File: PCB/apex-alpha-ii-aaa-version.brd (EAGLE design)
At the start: 13.1 x 74.7 mm, 31 parts, among them IC1 CC430F5135, Y1 26MHz

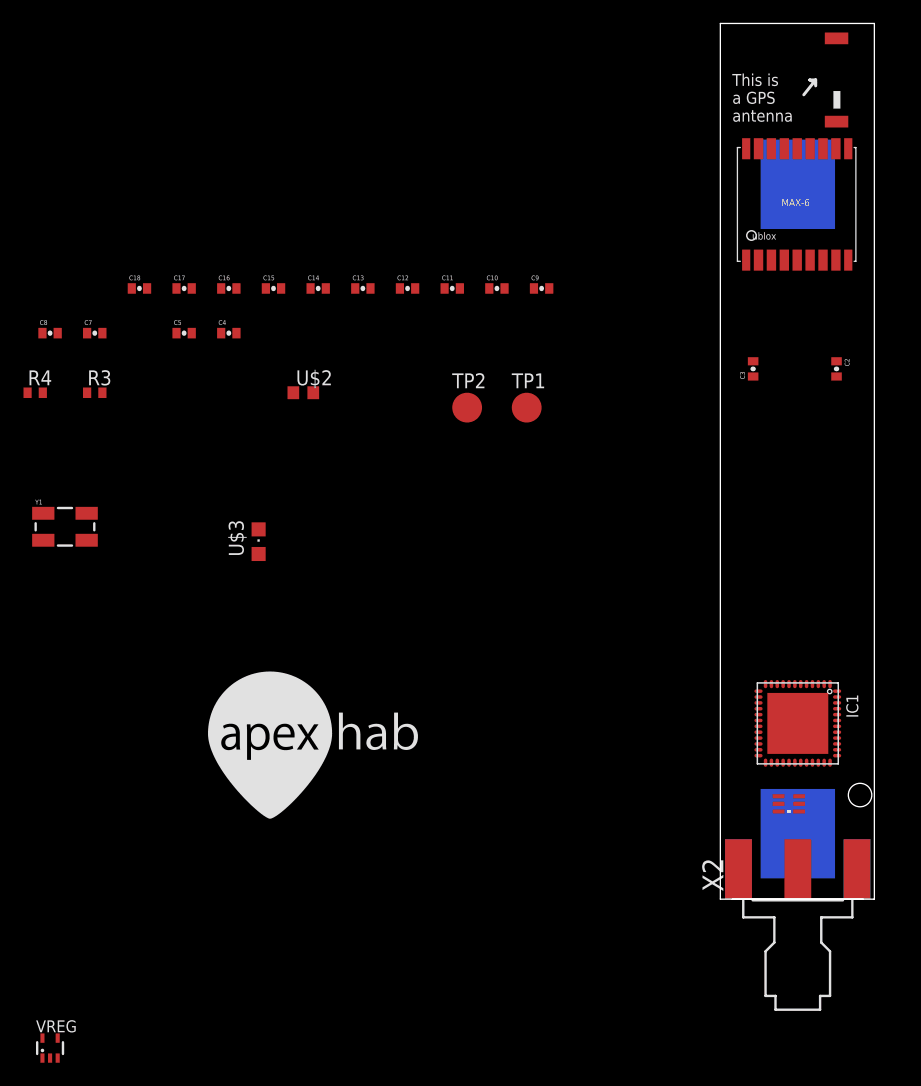
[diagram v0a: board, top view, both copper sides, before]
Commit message: Changed to TLV70019 linear reg for a 3V battery
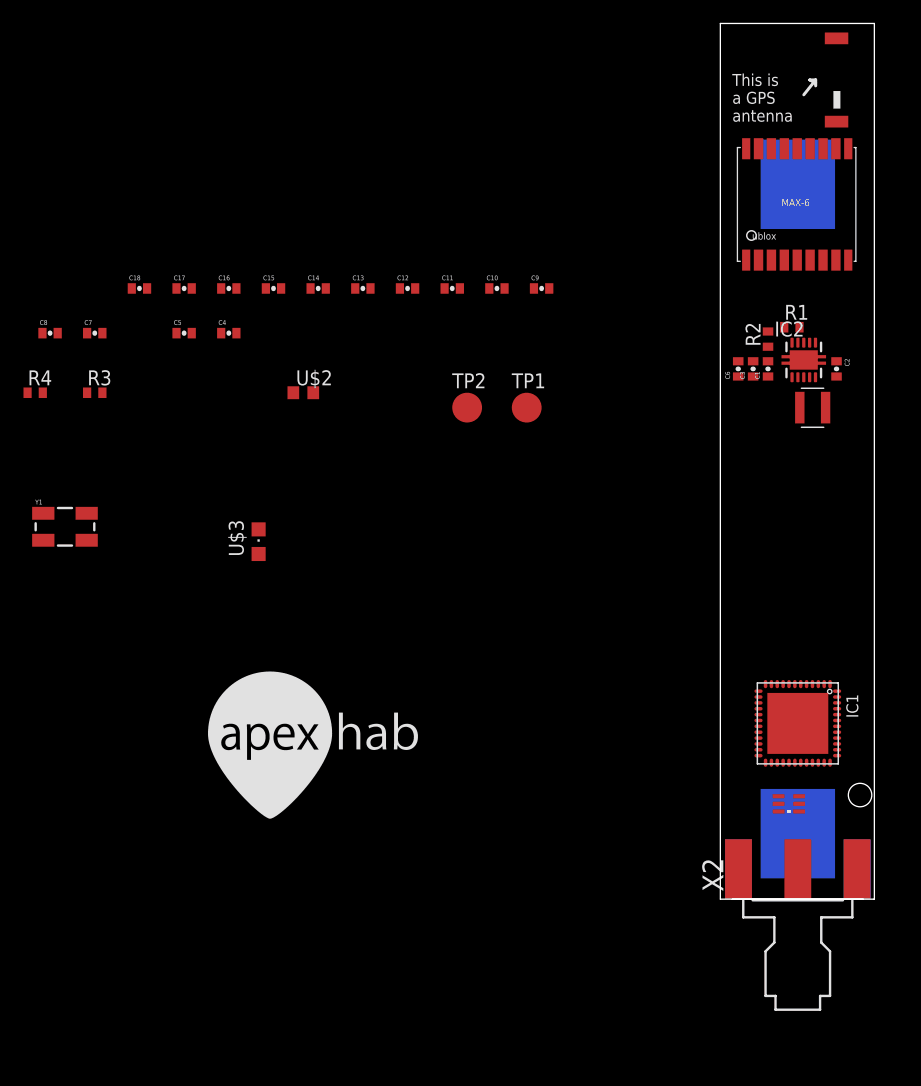
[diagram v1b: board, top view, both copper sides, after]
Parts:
- removed VREG: TLV70019, !danielparts:SC70-5L
- added C1: 1uF, apex:0402-CAP
- added C6: 100nF, apex:0402-CAP
- added IC2: TPS61200, texas:S-PDSO-N10
- added NR3015: 2.2uH, apex:NR3015
- added R1: 560k, apex:R0402
- added R2: 200k, apex:R0402
- C2, C3: value 1uF -> 10uF
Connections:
- new net N$1: AAA.+V, C2.2, IC2.5, IC2.6, IC2.7, IC2.8, NR3015.P$1
- new net N$4: IC2.10, R1.1, R2.2
- new net N$5: C1.1, IC2.1
- new net PP: IC2.PP, IC2.PP@1, IC2.PP@2
- net GND: now also C1.2, C6.2, IC2.4, IC2.9, R2.1; no longer VREG.2
- net N$3: now also IC2.3, NR3015.P$2; no longer AAA.+V, C2.2, VREG.1, VREG.3
- net VCC: now also C6.1, IC2.2, R1.2; no longer VREG.5

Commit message: AAA version fully laid out.
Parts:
- removed JP1: APEXHAB-LOGO_APEXHAB-SMALL, apex:APEXHAB-LOGO-SMALL
- added U$4: (no value), !danielparts:APEXHAB-LOGO-SMALL
- TP1, TP2: value PTR1B2,54 -> PTR1B1,27; device testpad:B2,54 -> testpad:B1,27
- moved C8 77.2 mm to (10.4, 10.9), turned to 270 degrees
- moved C7 72.7 mm to (11.9, 16.3), turned to 90 degrees
- moved R4 72.6 mm to (6.60, 10.9), turned to 90 degrees
- moved R3 65.8 mm to (4.06, 10.9), turned to 90 degrees
- moved C5 64.8 mm to (11.9, 18.8), turned to 90 degrees
- moved C4 62.2 mm to (7.87, 10.9), turned to 90 degrees
- moved C17 62.2 mm to (8.64, 21.8), turned to 270 degrees
- moved Y1 62.0 mm to (5.59, 23.6), turned to 90 degrees
- moved C18 58.2 mm to (8.64, 52.6), turned to 180 degrees
- moved C15 53.6 mm to (1.52, 16.0), turned to 180 degrees
- moved C12 52.1 mm to (5.33, 10.9), turned to 270 degrees
- moved U$3 52.0 mm to (11.9, 22.1)
- moved C16 50.8 mm to (1.52, 25.7), turned to 180 degrees
- moved C14 49.1 mm to (1.52, 18.5), turned to 180 degrees
- moved C9 47.8 mm to (9.14, 10.9), turned to 270 degrees
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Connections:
- new net VEE: C11.1, C12.1, C13.1, C14.1, C15.1, IC1.27, IC1.28, IC1.31, IC1.32, IC1.34, U$2.2
- net VCC: no longer C11.1, C12.1, C13.1, C14.1, C15.1, IC1.27, IC1.28, IC1.31, IC1.32, IC1.34, U$2.2
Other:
- board text added: "APEX ALPHA Mk II"
- board text removed: "This is a GPS antenna"

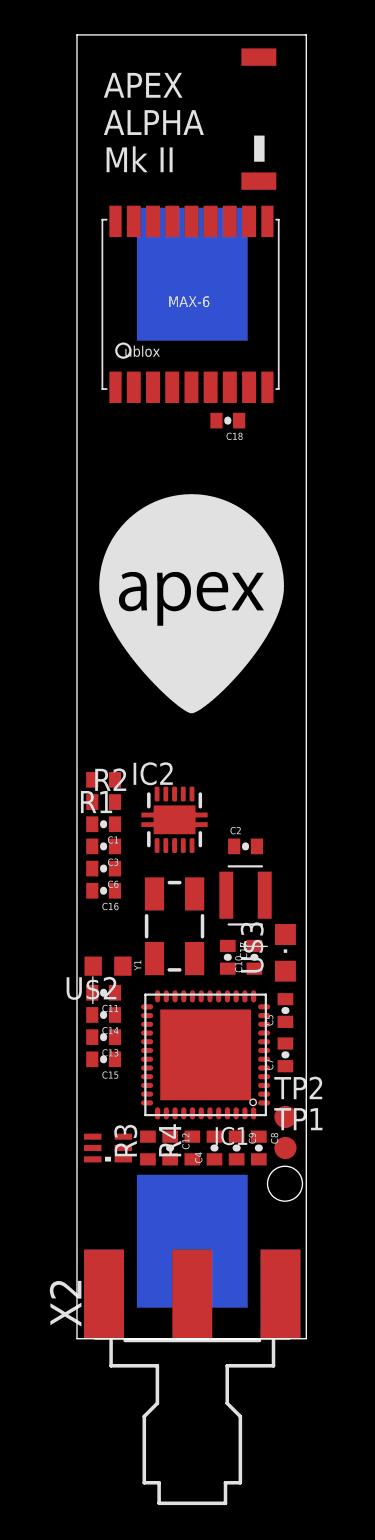
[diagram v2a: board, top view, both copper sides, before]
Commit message: Ground planes. Started routing.
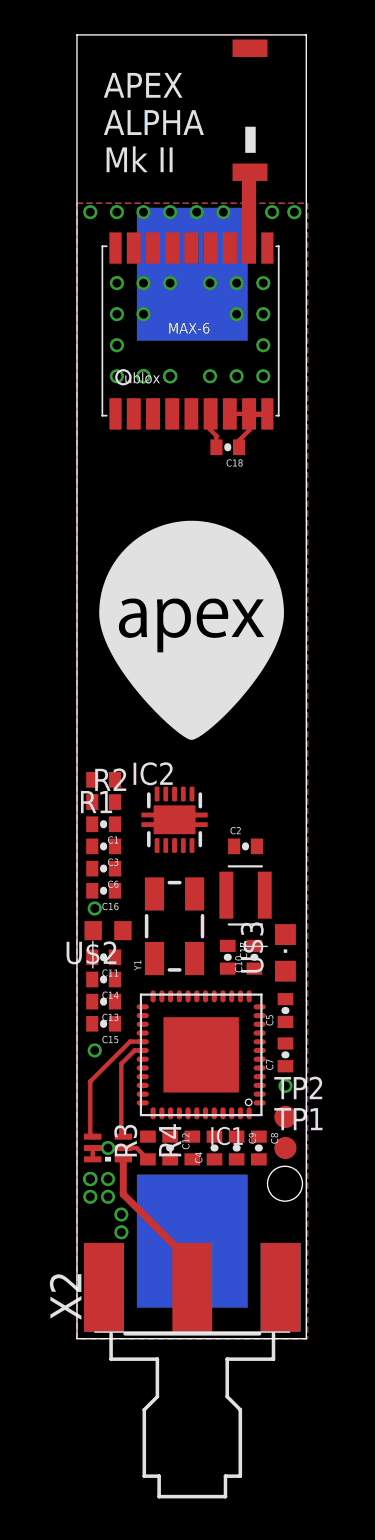
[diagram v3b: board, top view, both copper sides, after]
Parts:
- moved C11 2.03 mm to (1.52, 21.8)
- moved C13 2.03 mm to (1.52, 19.3)
- moved C14 2.03 mm to (1.52, 20.6)
- moved C15 2.03 mm to (1.52, 18.0)
- moved U$2 2.03 mm to (1.78, 23.4)
- moved C18 1.52 mm to (8.64, 51.1)
- moved GPS 1.52 mm to (6.60, 57.9)
- moved U$4 1.52 mm to (1.27, 34.3)
- moved U$1 0.72 mm to (8.64, 70.6)
- moved X2 0.38 mm to (6.60, 0.38)
- moved IC1 0.25 mm to (7.11, 16.3)
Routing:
- net GND: track 0.00 -> 9.84 mm, vias 0 -> 39
- net N$7: track 0.00 -> 8.96 mm
- net N$6: track 0.00 -> 7.19 mm
- net N$2: track 0.00 -> 5.76 mm
- net VCC: track 0.00 -> 5.36 mm
- net N$8: track 0.00 -> 4.36 mm
- added copper zone on layer 1, net GND
- added copper zone on layer 16, net GND

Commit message: Nearly finished routing... committing before I lose it all.
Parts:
- U$3: device apex:CHIPLED_0805 -> apex:CHIPLED_0603
- moved U$3 8.64 mm to (11.9, 13.5), turned to 180 degrees
- moved TP2 7.41 mm to (5.59, 8.89)
- moved TP1 4.77 mm to (7.62, 8.89)
- moved C5 3.05 mm to (11.9, 21.8)
- moved C7 2.79 mm to (11.9, 19.1), turned to 270 degrees
- moved F1 2.79 mm to (1.78, 8.13)
- moved R4 2.55 mm to (9.14, 11.2)
- moved R3 1.55 mm to (2.54, 11.2)
- moved C12 1.55 mm to (3.81, 11.2)
- moved C8 1.30 mm to (11.7, 11.2)
- moved C9 1.30 mm to (10.4, 11.2)
- moved U$4 0.76 mm to (1.27, 35.1)
- moved R1 0.25 mm to (1.52, 32.3)
- moved C1 0.25 mm to (1.52, 29.7)
- moved C16 0.25 mm to (1.52, 25.9)
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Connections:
- removed net PP: IC2.PP, IC2.PP@1, IC2.PP@2
- net GND: now also IC2.PP, IC2.PP@1, IC2.PP@2
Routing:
- net GND: track 9.84 -> 88.4 mm, vias 39 -> 42
- net VCC: track 5.36 -> 81.1 mm
- net GPSRX: track 0.00 -> 48.0 mm, vias 0 -> 2
- net GPSTX: track 0.00 -> 46.7 mm, vias 0 -> 2
- net N$1: track 0.00 -> 38.5 mm, vias 0 -> 1
- net VEE: track 0.00 -> 17.5 mm
- net N$14: track 0.00 -> 10.7 mm
- net N$11: track 0.00 -> 8.28 mm
- net N$13: track 0.00 -> 7.21 mm
- net N$3: track 0.00 -> 4.81 mm
- net N$9: track 0.00 -> 4.45 mm
- net N$12: track 0.00 -> 4.13 mm
- net N$4: track 0.00 -> 3.75 mm
- net N$2: track 5.76 -> 9.40 mm
- net N$6: track 7.19 -> 10.2 mm
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
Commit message: Finished! I think.
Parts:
- U$3: device apex:CHIPLED_0603 -> apex:R0402
- moved U$3 0.25 mm to (11.7, 13.5), turned to 90 degrees
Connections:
- net GND: now also U$3.1; no longer U$3.C
- net N$15: now also U$3.2; no longer U$3.A
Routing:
- net N$15: track 0.00 -> 1.47 mm
- net GND: track 88.4 -> 89.7 mm
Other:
- board text added: ">"
- board text added: "DANIEL"
- board text added: "Dec 2012"
- board text added: "SAUL"
- board text added: "You need to put a battery here."
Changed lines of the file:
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@@
 <setting verticaltext="up"/>
 </settings>
-<grid distance="0.01" unitdist="inch" unit="inch" style="dots" multiple="1" display="yes" altdistance="0.005" altunitdist="inch" altunit="inch"/>
+<grid distance="0.01" unitdist="inch" unit="inch" style="dots" multiple="1" display="yes" altdistance="0.001" altunitdist="inch" altunit="inch"/>
 <layers>
 <layer number="1" name="Top" color="4" fill="1" visible="yes" active="yes"/>
@@
 <layer number="39" name="tKeepout" color="4" fill="11" visible="no" active="yes"/>
 <layer number="40" name="bKeepout" color="1" fill="11" visible="no" active="yes"/>
-<layer number="41" name="tRestrict" color="4" fill="10" visible="yes" active="yes"/>
+<layer number="41" name="tRestrict" color="4" fill="10" visible="no" active="yes"/>
 <layer number="42" name="bRestrict" color="1" fill="10" visible="no" active="yes"/>
 <layer number="43" name="vRestrict" color="2" fill="10" visible="no" active="yes"/>
@@
 <wire x1="13.132" y1="74.666" x2="0" y2="74.666" width="0" layer="20"/>
 <wire x1="0" y1="74.666" x2="0" y2="0" width="0" layer="20"/>
-<text x="1.524" y="66.802" size="1.4224" layer="21" font="vector" ratio="15">APEX
+<text x="1.524" y="67.056" size="1.4224" layer="21" font="vector" ratio="15">APEX
 ALPHA
 Mk II</text>
+<text x="6.096" y="17.018" size="1.27" layer="22" font="vector" ratio="15" rot="MR90">You need to put a battery here.</text>
+<text x="10.922" y="71.374" size="1.778" layer="22" font="vector" ratio="15" rot="MR0">DANIEL</text>
+<text x="9.652" y="68.58" size="1.778" layer="22" font="vector" ratio="15" rot="MR0">SAUL</text>
+<text x="10.414" y="66.04" size="1.016" layer="22" font="vector" ratio="15" rot="MR0">Dec 2012</text>
+<text x="11.3792" y="13.6652" size="0.6096" layer="21" font="vector" ratio="15" rot="SR270">&gt;</text>
 </plain>
 <attributes>
@@
 <element name="C17" library="apex" package="0402-CAP" value="27pF" x="8.636" y="21.844" rot="R270"/>
 <element name="U$2" library="apex" package="R0603" value="EXC3BB601H" x="1.651" y="23.368" rot="R180"/>
-<element name="U$3" library="apex" package="CHIPLED_0603" value="STATUS" x="11.938" y="13.462" rot="R180"/>
+<element name="U$3" library="apex" package="R0402" value="STATUS" x="11.684" y="13.462" rot="R90"/>
 <element name="C18" library="apex" package="0402-CAP" value="100nF" x="8.636" y="51.054" rot="R180"/>
 <element name="U$4" library="!danielparts" package="APEXHAB-LOGO-SMALL" value="" x="1.27" y="35.052"/>
@@
 <contactref element="C17" pad="1"/>
 <contactref element="GPS" pad="1_GND"/>
-<contactref element="U$3" pad="C"/>
+<contactref element="U$3" pad="1"/>
 <contactref element="GPS" pad="6_V_BCKP"/>
 <contactref element="C18" pad="2"/>
@@
 <wire x1="10.414" y1="10.526" x2="12.558" y2="10.526" width="0.254" layer="1"/>
 <wire x1="12.558" y1="10.526" x2="12.7" y2="10.668" width="0.254" layer="1"/>
-<wire x1="12.7" y1="10.668" x2="12.7" y2="20.574" width="0.254" layer="1"/>
+<wire x1="12.7" y1="10.668" x2="12.7" y2="13.462" width="0.254" layer="1"/>
+<wire x1="12.7" y1="13.462" x2="12.7" y2="20.574" width="0.254" layer="1"/>
 <wire x1="0.874" y1="28.448" x2="0.874" y2="27.178" width="0.254" layer="1"/>
 <wire x1="0.874" y1="27.178" x2="0.874" y2="25.908" width="0.254" layer="1"/>
@@
 <via x="2.032" y="33.782" extent="1-16" drill="0.508"/>
 <via x="5.588" y="29.972" extent="1-16" drill="0.508"/>
+<wire x1="11.684" y1="12.812" x2="12.05" y2="12.812" width="0.254" layer="1"/>
+<wire x1="12.05" y1="12.812" x2="12.7" y2="13.462" width="0.254" layer="1"/>
 <wire x1="5.588" y1="29.972" x2="5.588" y2="30.247" width="0" layer="19" extent="1-1"/>
 <wire x1="5.588" y1="29.697" x2="5.588" y2="29.718" width="0" layer="19" extent="1-1"/>
-<wire x1="11.938" y1="12.712" x2="12.7" y2="10.668" width="0" layer="19" extent="1-1"/>
 </signal>
 <signal name="N$1">
@@
 <signal name="N$15">
 <contactref element="IC1" pad="1"/>
-<contactref element="U$3" pad="A"/>
-<wire x1="10.462" y1="13.506" x2="11.938" y2="14.212" width="0" layer="19" extent="1-1"/>
+<contactref element="U$3" pad="2"/>
+<wire x1="10.462" y1="13.506" x2="11.078" y2="13.506" width="0.254" layer="1"/>
+<wire x1="11.078" y1="13.506" x2="11.684" y2="14.112" width="0.254" layer="1"/>
 </signal>
 <signal name="GPSRX">

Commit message: New PCB layout etc.
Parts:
- removed U$4: (no value), !danielparts:APEXHAB-LOGO-SMALL
- added C19: 4.7uF, apex:0805
- AAA: device apex:SMD-BATTERY-HOLDER-AAA -> apex:THROUGH-HOLE-BATTERY-HOLDER-AAA
- C10: value 10uF -> 1uF
- C2, C3: device apex:0402-CAP -> apex:0805
- C9: value 10uF -> 100nF
- moved C16 19.3 mm to (4.83, 6.86), turned to 270 degrees
- moved Y1 15.6 mm to (2.29, 8.64), turned to 270 degrees
- moved C18 15.2 mm to (8.76, 35.8), turned to 270 degrees
- moved C9 15.0 mm to (4.06, 24.8), turned to 90 degrees
- moved GPS 14.5 mm to (6.60, 43.4)
- moved C11 13.7 mm to (11.9, 13.0), turned to 270 degrees
- moved U$1 13.0 mm to (8.64, 57.7)
- moved C8 12.9 mm to (1.52, 19.1), turned to 90 degrees
- moved C14 11.7 mm to (10.4, 13.0), turned to 270 degrees
- moved C17 11.4 mm to (1.52, 13.0)
- moved U$3 11.2 mm to (8.76, 24.3), turned to 0 degrees
- moved NR3015 9.76 mm to (3.56, 33.3), turned to 180 degrees
- moved R1 9.33 mm to (9.65, 27.7), turned to 0 degrees
- moved C3 9.07 mm to (10.4, 30.2), turned to 270 degrees
- moved C7 8.54 mm to (5.59, 24.8)
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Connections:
- net GND: now also C19.2
- net VCC: now also C19.1
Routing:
- net GND: track 89.7 -> 1.41 mm, vias 42 -> 32
- net GPSRX: track 48.0 -> 0.00 mm, vias 2 -> 0
- net GPSTX: track 46.7 -> 0.00 mm, vias 2 -> 0
- net VCC: track 81.1 -> 58.7 mm, vias 0 -> 3
- net N$1: track 38.5 -> 21.9 mm, vias 1 -> 0
- net N$6: track 10.2 -> 0.85 mm
- net N$2: track 9.40 -> 0.84 mm
- net N$12: track 4.13 -> 11.4 mm, vias 0 -> 2
- net VEE: track 17.5 -> 13.9 mm
- net N$13: track 7.21 -> 9.90 mm
- net N$7: track 6.63 -> 9.18 mm
- net N$3: track 4.81 -> 2.66 mm
- net N$9: track 4.45 -> 2.40 mm
- net N$11: track 8.28 -> 10.1 mm, vias 0 -> 2
- net N$8: track 4.36 -> 5.89 mm
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- added copper zone on layer 1, net N$1
- added copper zone on layer 1, net N$2
- added copper zone on layer 1, net N$6
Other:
- board size 13.1 x 74.7 mm -> 13.1 x 62.2 mm
- board text added: "ALPHA"
- board text added: "APEX"
- board text added: "Mk II"
- board text removed: ">"
- board text removed: "APEX ALPHA Mk II"
- board text removed: "DANIEL"
- board text removed: "Dec 2012"
- board text removed: "SAUL"
- board text removed: "You need to put a battery here."
